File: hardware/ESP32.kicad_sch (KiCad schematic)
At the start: 17 parts, among them J1 GT-USB-7004, SW1 SW_Omron_B3FS, SW2 SW_Omron_B3FS, U1 ESP32-C3-WROOM-02U, U2 VBUS05L1-DD1-G-08, U3 VBUS05L1-DD1-G-08, U4 VBUS05L1-DD1-G-08

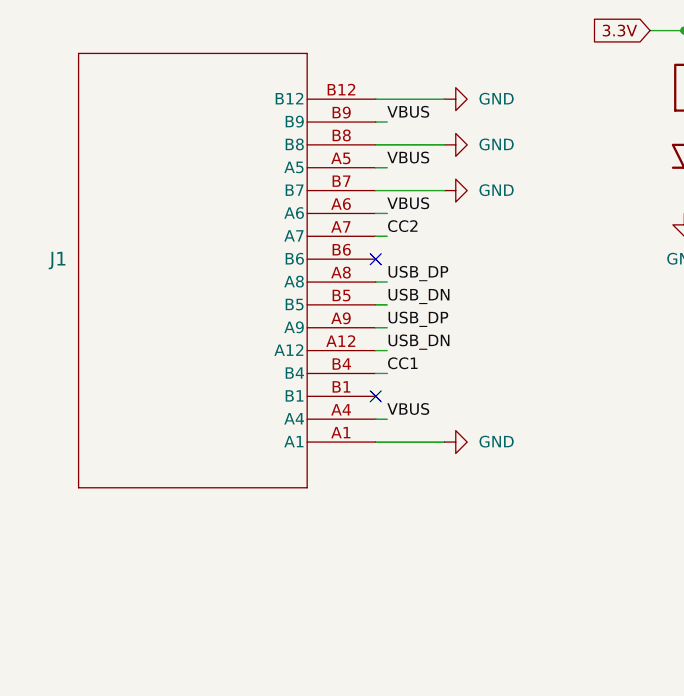
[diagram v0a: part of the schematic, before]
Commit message: New usb port
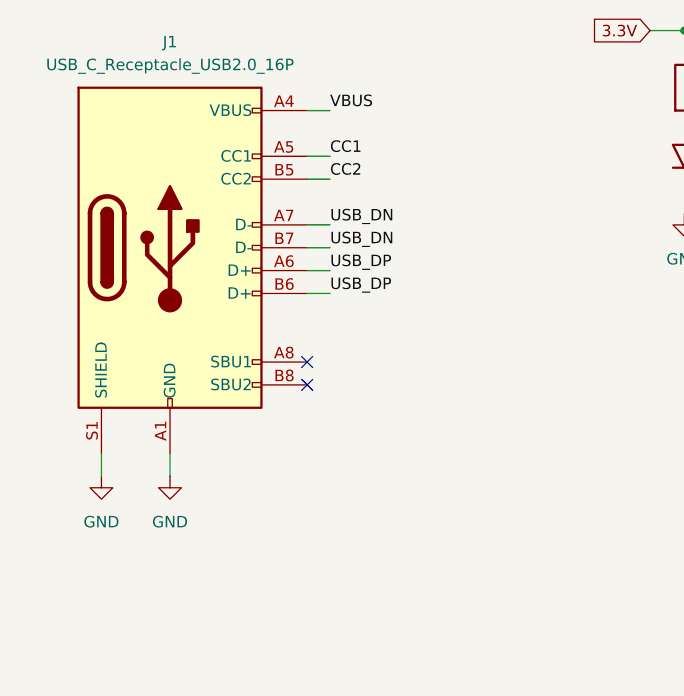
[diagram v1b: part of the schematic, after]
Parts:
- removed J1: GT-USB-7004, GT-USB-7004:CONN12_B-7004_GSW, symbol GT-USB-7004:GT-USB-7004
- added J1: USB_C_Receptacle_USB2.0_16P, Connector_USB:USB_C_Receptacle_GCT_USB4105-xx-A_16P_TopMnt_Horizontal, symbol Connector:USB_C_Receptacle_USB2.0_16P
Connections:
- net CC1: now also J1.A5 (CC1)
- net CC2: now also J1.B5 (CC2)
- net GND: now also J1.A1 (GND), J1.A12 (GND), J1.B1 (GND), J1.B12 (GND), J1.S1 (SHIELD)
- net USB_DN: now also J1.A7 (D-), J1.B7 (D-)
- net USB_DP: now also J1.A6 (D+), J1.B6 (D+)
- net VBUS: now also J1.A4 (VBUS), J1.A9 (VBUS), J1.B4 (VBUS), J1.B9 (VBUS)

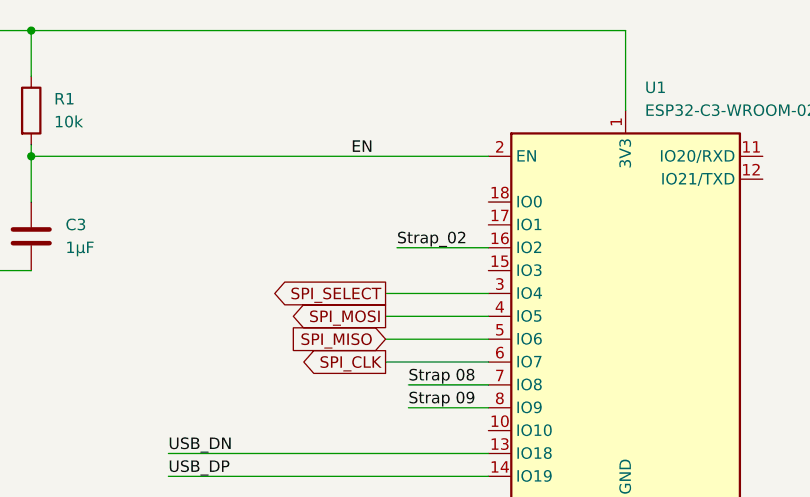
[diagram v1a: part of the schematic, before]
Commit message: Main modules added + Com lines
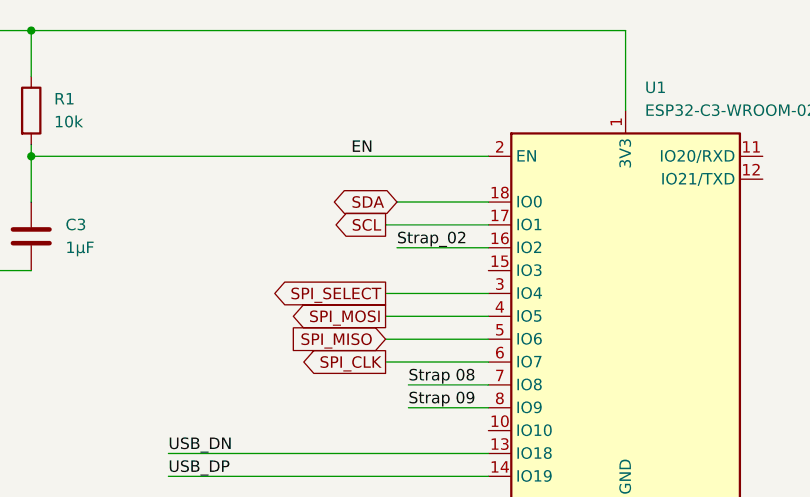
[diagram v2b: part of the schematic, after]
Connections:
- net SCL: now reaches U1.17 (IO1)
- net SDA: now reaches U1.18 (IO0)
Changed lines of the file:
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@@
+	(wire
+		(pts
+			(xy 187.96 50.8) (xy 198.12 50.8)
+		)
+		(stroke
+			(width 0)
+			(type default)
+		)
+	)
 	(wire
 		(pts
@@
 		(pts
 			(xy 129.54 49.53) (xy 134.62 49.53)
+		)
+		(stroke
+			(width 0)
+			(type default)
+		)
+	)
+	(wire
+		(pts
+			(xy 186.69 53.34) (xy 198.12 53.34)
 		)
 		(stroke
@@
 		)
 	)
+	(global_label "SCL"
+		(shape output)
+		(at 186.69 53.34 180)
+		(fields_autoplaced yes)
+		(effects
+			(font
+				(size 1.27 1.27)
+			)
+			(justify right)
+		)
+		(property "Intersheetrefs" "${INTERSHEET_REFS}"
+			(at 180.1972 53.34 0)
+			(effects
+				(font
+					(size 1.27 1.27)
+				)
+				(justify right)
+				(hide yes)
+			)
+		)
+	)
 	(global_label "SPI_MISO"
 		(shape input)
@@
 			(effects
 				(font
+					(size 1.27 1.27)
+				)
+				(justify right)
+				(hide yes)
+			)
+		)
+	)
+	(global_label "SDA"
+		(shape bidirectional)
+		(at 187.96 50.8 180)
+		(fields_autoplaced yes)
+		(effects
+			(font
+				(size 1.27 1.27)
+			)
+			(justify right)
+		)
+		(property "Intersheetrefs" "${INTERSHEET_REFS}"
+			(at 180.2954 50.8 0)
+			(effects
+				(font

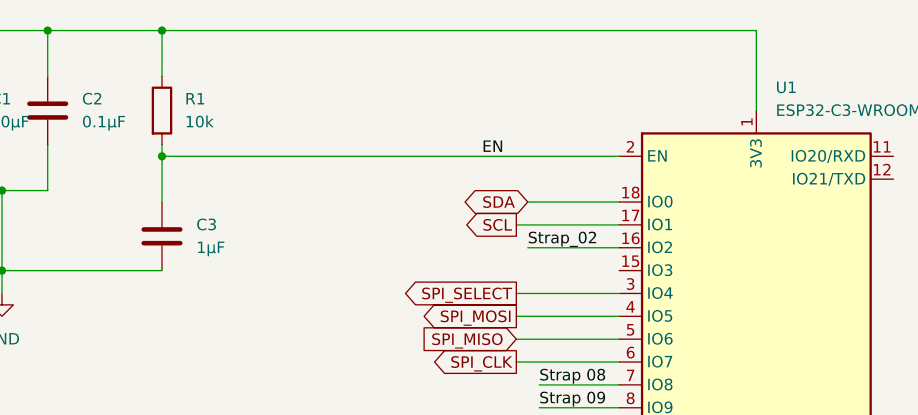
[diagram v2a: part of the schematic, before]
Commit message: Pull up resistor i2c
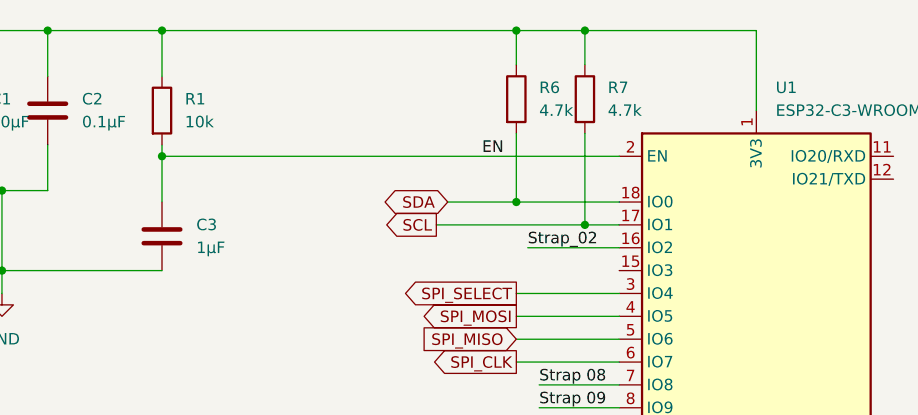
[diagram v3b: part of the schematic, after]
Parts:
- added R6, R7: 4.7k, Resistor_SMD:R_0603_1608Metric, symbol Device:R
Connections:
- net 3.3V: now also R6.1, R7.1
- net SCL: now also R7.2
- net SDA: now also R6.2
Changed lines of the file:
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@@
+	)
+	(junction
+		(at 194.31 31.75)
+		(diameter 0)
+		(color 0 0 0 0)
 	)
 	(junction
@@
 	)
 	(junction
+		(at 194.31 53.34)
+		(diameter 0)
+		(color 0 0 0 0)
+	)
+	(junction
+		(at 186.69 50.8)
+		(diameter 0)
+		(color 0 0 0 0)
+	)
+	(junction
 		(at 124.46 31.75)
 		(diameter 0)
@@
 	)
 	(junction
+		(at 186.69 31.75)
+		(diameter 0)
+		(color 0 0 0 0)
+	)
+	(junction
 		(at 134.62 31.75)
 		(diameter 0)
@@
 	(wire
 		(pts
+			(xy 186.69 31.75) (xy 147.32 31.75)
+		)
+		(stroke
+			(width 0)
+			(type default)
+		)
+	)
+	(wire
+		(pts
+			(xy 186.69 43.18) (xy 186.69 50.8)
+		)
+		(stroke
+			(width 0)
+			(type default)
+		)
+	)
+	(wire
+		(pts
 			(xy 105.41 31.75) (xy 114.3 31.75)
 		)
@@
 	(wire
 		(pts
+			(xy 194.31 31.75) (xy 186.69 31.75)
+		)
+		(stroke
+			(width 0)
+			(type default)
+		)
+	)
+	(wire
+		(pts
 			(xy 162.56 78.74) (xy 198.12 78.74)
 		)
@@
 	(wire
 		(pts
-			(xy 213.36 31.75) (xy 147.32 31.75)
+			(xy 213.36 31.75) (xy 194.31 31.75)
 		)
 		(stroke
@@
 	(wire
 		(pts
-			(xy 187.96 50.8) (xy 198.12 50.8)
+			(xy 179.07 50.8) (xy 186.69 50.8)
 		)
 		(stroke
@@
 	(wire
 		(pts
-			(xy 186.69 53.34) (xy 198.12 53.34)
+			(xy 194.31 31.75) (xy 194.31 35.56)
+		)
+		(stroke
+			(width 0)
+			(type default)
+		)
+	)
+	(wire
+		(pts
+			(xy 177.8 53.34) (xy 194.31 53.34)
+		)
+		(stroke
+			(width 0)
+			(type default)
+		)
+	)
+	(wire
+		(pts
+			(xy 186.69 31.75) (xy 186.69 35.56)
 		)
 		(stroke
@@
 	(wire
 		(pts
+			(xy 186.69 50.8) (xy 198.12 50.8)
+		)
+		(stroke
+			(width 0)
+			(type default)
+		)
+	)
+	(wire
+		(pts
+			(xy 194.31 43.18) (xy 194.31 53.34)
+		)
+		(stroke
+			(width 0)
+			(type default)
+		)
+	)
+	(wire
+		(pts
 			(xy 186.69 63.5) (xy 198.12 63.5)
 		)
@@
 		(pts
 			(xy 147.32 36.83) (xy 147.32 31.75)
+		)
+		(stroke
+			(width 0)
+			(type default)
+		)
+	)
+	(wire
+		(pts
+			(xy 194.31 53.34) (xy 198.12 53.34)
 		)
 		(stroke
@@
 	(global_label "SCL"
 		(shape output)
-		(at 186.69 53.34 180)
+		(at 177.8 53.34 180)
 		(fields_autoplaced yes)
 		(effects
@@
 		)
 		(property "Intersheetrefs" "${INTERSHEET_REFS}"
-			(at 180.1972 53.34 0)
+			(at 171.3072 53.34 0)
 			(effects
 				(font
@@
 	(global_label "SDA"
 		(shape bidirectional)
-		(at 187.96 50.8 180)
+		(at 179.07 50.8 180)
 		(fields_autoplaced yes)
 		(effects
@@
 		)
 		(property "Intersheetrefs" "${INTERSHEET_REFS}"
-			(at 180.2954 50.8 0)
+			(at 171.4054 50.8 0)
 			(effects
 				(font
@@
 				(path "/5b969f6e-a36e-432b-8f00-b2d6a515a877/36e0c9fb-3d9d-4ab1-92fc-4f7433c1320d"
 					(reference "#PWR02")
+					(unit 1)
+				)
+			)
+		)
+	)
+	(symbol
+		(lib_id "Device:R")
+		(at 186.69 39.37 0)
+		(unit 1)
+		(exclude_from_sim no)
+		(in_bom yes)
+		(on_board yes)
+		(dnp no)
+		(fields_autoplaced yes)
+		(property "Reference" "R6"
+			(at 189.23 38.0999 0)
+			(effects
+				(font
+					(size 1.27 1.27)
+				)
+				(justify left)
+			)
+		)
+		(property "Value" "4.7k"
+			(at 189.23 40.6399 0)
+			(effects
+				(font
+					(size 1.27 1.27)
+				)
+				(justify left)
+			)
+		)
+		(property "Footprint" "Resistor_SMD:R_0603_1608Metric"
+			(at 184.912 39.37 90)
+			(effects
+				(font
+					(size 1.27 1.27)
+				)
+				(hide yes)
+			)
+		)
+		(property "Datasheet" "~"
+			(at 186.69 39.37 0)
+			(effects
+				(font
+					(size 1.27 1.27)
+				)
+				(hide yes)
+			)
+		)
+		(property "Description" "Resistor"
+			(at 186.69 39.37 0)
+			(effects
+				(font
+					(size 1.27 1.27)
+				)
+				(hide yes)
+			)
+		)
+		(pin "2"
+		)
+		(pin "1"
+		)
+		(instances
+			(project "GOG"
+				(path "/5b969f6e-a36e-432b-8f00-b2d6a515a877/36e0c9fb-3d9d-4ab1-92fc-4f7433c1320d"
+					(reference "R6")
 					(unit 1)
 				)
@@
 					(unit 1)
 				)
+			)
+		)
+	)
+	(symbol
+		(lib_id "Device:R")
+		(at 194.31 39.37 0)
+		(unit 1)
+		(exclude_from_sim no)
+		(in_bom yes)
+		(on_board yes)
+		(dnp no)
+		(fields_autoplaced yes)
+		(property "Reference" "R7"
+			(at 196.85 38.0999 0)
+			(effects
+				(font
+					(size 1.27 1.27)
+				)
+				(justify left)
+			)
+		)
+		(property "Value" "4.7k"
+			(at 196.85 40.6399 0)
+			(effects
+				(font
+					(size 1.27 1.27)
+				)
+				(justify left)
+			)
+		)
+		(property "Footprint" "Resistor_SMD:R_0603_1608Metric"
+			(at 192.532 39.37 90)
+			(effects
+				(font
+					(size 1.27 1.27)
+				)
+				(hide yes)
+			)
+		)
+		(property "Datasheet" "~"
+			(at 194.31 39.37 0)
+			(effects
+				(font
+					(size 1.27 1.27)
+				)
+				(hide yes)
+			)
+		)
+		(property "Description" "Resistor"
+			(at 194.31 39.37 0)
+			(effects
+				(font
+					(size 1.27 1.27)
+				)
+				(hide yes)
+			)
+		)
+		(pin "2"
+		)
+		(pin "1"
+		)
+		(instances
+			(project "GOG"
+				(path "/5b969f6e-a36e-432b-8f00-b2d6a515a877/36e0c9fb-3d9d-4ab1-92fc-4f7433c1320d"
+					(reference "R7")
+					(unit 1)
+				)

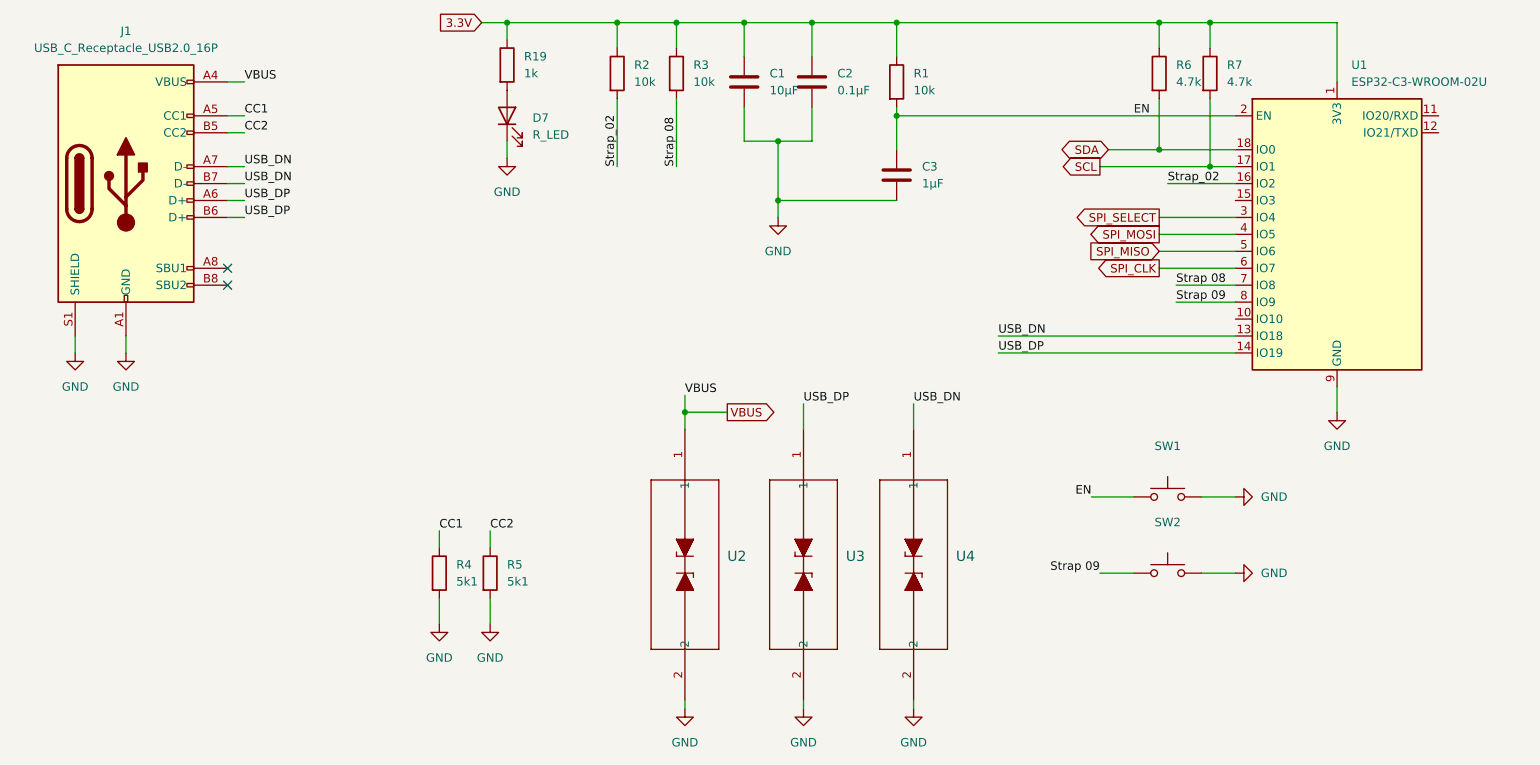
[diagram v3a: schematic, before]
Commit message: ESL protection modification with usblc6 2sc6
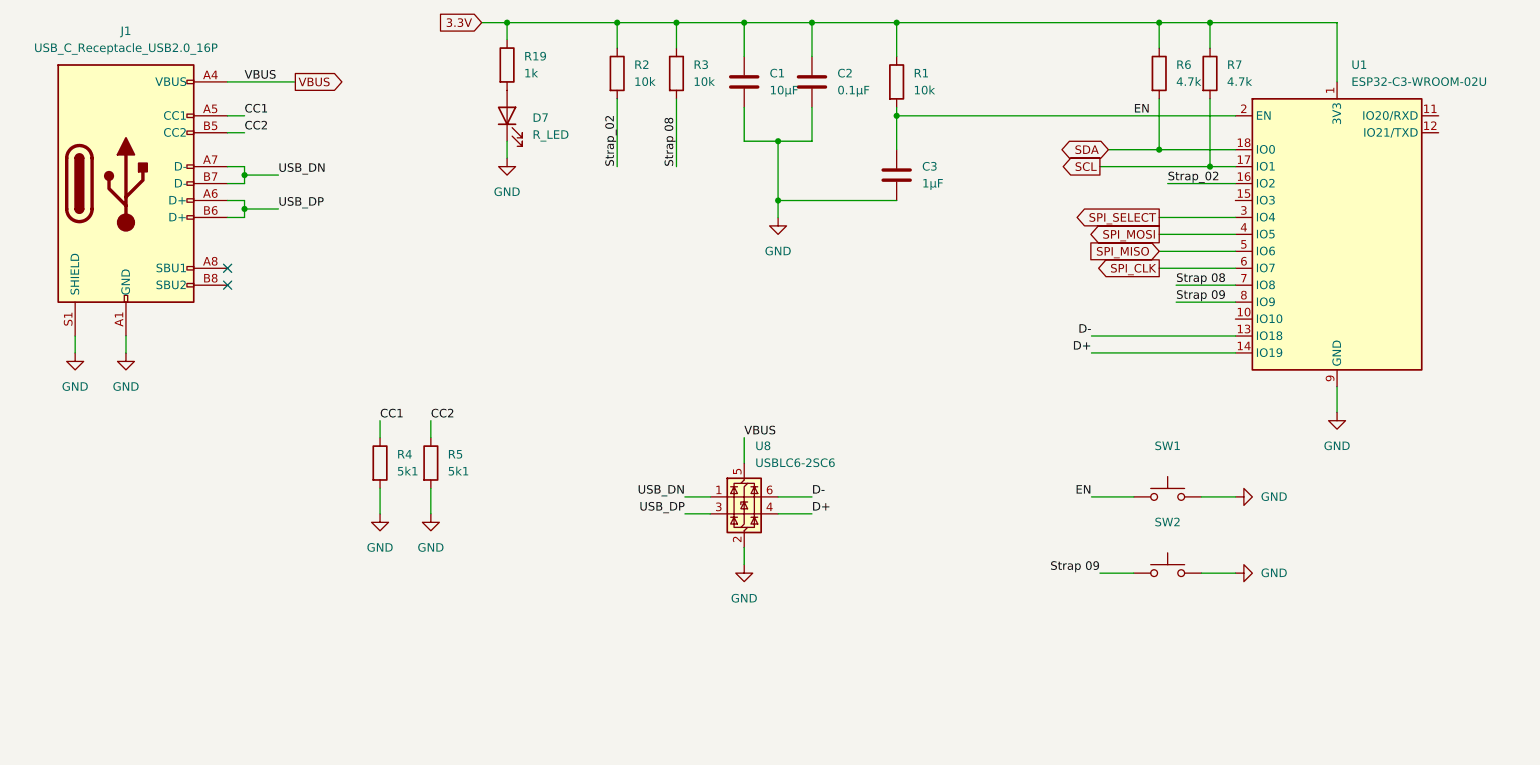
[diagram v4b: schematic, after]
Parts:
- removed U2, U3, U4: VBUS05L1-DD1-G-08, VBUS05L1-DD1-G-08:DIO_LLP1006-2M_VIS, symbol VBUS05L1-DD1-G-08:VBUS05L1-DD1-G-08
- added U8: USBLC6-2SC6, Package_TO_SOT_SMD:SOT-23-6, symbol Power_Protection:USBLC6-2SC6
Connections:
- net GND: now also U8.2 (GND)
- net USB_DN: now also U8.1 (I/O1); no longer U1.13 (IO18)
- net USB_DP: now also U8.3 (I/O2); no longer U1.14 (IO19)
- net VBUS: now also U8.5 (VBUS)
- new net D+: U1.14 (IO19), U8.4 (I/O2)
- new net D-: U1.13 (IO18), U8.6 (I/O1)
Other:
- moved on the sheet: R4, R5

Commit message: Change of esp32 footprint for wifi antenna
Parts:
- removed U1: ESP32-C3-WROOM-02U, RF_Module:ESP32-C3-WROOM-02U, symbol RF_Module:ESP32-C3-WROOM-02U
- added U2: ESP32-C3-WROOM-02, RF_Module:ESP32-C3-WROOM-02, symbol RF_Module:ESP32-C3-WROOM-02
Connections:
- net 3.3V: now also U2.1 (3V3)
- net D+: now also U2.14 (IO19)
- net D-: now also U2.13 (IO18)
- net EN: now also U2.2 (EN)
- net GND: now also U2.19 (GND), U2.9 (GND)
- net SCL: now also U2.17 (IO1)
- net SDA: now also U2.18 (IO0)
- net SPI_CLK: now also U2.6 (IO7)
- net SPI_MISO: now also U2.5 (IO6)
- net SPI_MOSI: now also U2.4 (IO5)
- net SPI_SELECT: now also U2.3 (IO4)
- net Strap 08: now also U2.7 (IO8)
- net Strap 09: now also U2.8 (IO9)
- net Strap_02: now also U2.16 (IO2)
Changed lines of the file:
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@@
-	)
-	(symbol
-		(lib_id "RF_Module:ESP32-C3-WROOM-02U")
-		(at 213.36 63.5 0)
-		(unit 1)
-		(exclude_from_sim no)
-		(in_bom yes)
-		(on_board yes)
-		(dnp no)
-		(fields_autoplaced yes)
-		(property "Reference" "U1"
-			(at 215.5033 38.1 0)
-			(effects
-				(font
-					(size 1.27 1.27)
-				)
-				(justify left)
-			)
-		)
-		(property "Value" "ESP32-C3-WROOM-02U"
-			(at 215.5033 40.64 0)
-			(effects
-				(font
-					(size 1.27 1.27)
-				)
-				(justify left)
-			)
-		)
-		(property "Footprint" "RF_Module:ESP32-C3-WROOM-02U"
-			(at 213.36 64.135 0)
-			(effects
-				(font
-					(size 1.27 1.27)
-				)
-				(hide yes)
-			)
-		)
-		(property "Datasheet" "https://www.espressif.com/sites/default/files/documentation/esp32-c3-wroom-02_datasheet_en.pdf"
-			(at 213.36 64.135 0)
-			(effects
-				(font
-					(size 1.27 1.27)
-				)
-				(hide yes)
-			)
-		)
-		(property "Description" "802.11 b/g/n Wi­Fi and Bluetooth 5 module, ESP32­C3 SoC, RISC­V microprocessor, On-board antenna"
-			(at 213.36 64.135 0)
-			(effects
-				(font
-					(size 1.27 1.27)
-				)
-				(hide yes)
-			)
-		)
-		(pin "3"
-		)
-		(pin "2"
-		)
-		(pin "18"
-		)
-		(pin "17"
-		)
-		(pin "5"
-		)
-		(pin "4"
-		)
-		(pin "10"
-		)
-		(pin "8"
-		)
-		(pin "15"
-		)
-		(pin "7"
-		)
-		(pin "16"
-		)
-		(pin "6"
-		)
-		(pin "14"
-		)
-		(pin "1"
-		)
-		(pin "13"
-		)
-		(pin "19"
-		)
-		(pin "11"
-		)
-		(pin "9"
-		)
-		(pin "12"
-		)
-		(instances
-			(project ""
-				(path "/5b969f6e-a36e-432b-8f00-b2d6a515a877/36e0c9fb-3d9d-4ab1-92fc-4f7433c1320d"
-					(reference "U1")
-					(unit 1)
-				)
-			)
-		)
 	)
 	(symbol
@@
 					(unit 1)
 				)
+			)
+		)
+	)
+	(symbol
+		(lib_id "RF_Module:ESP32-C3-WROOM-02")
+		(at 213.36 63.5 0)
+		(unit 1)
+		(exclude_from_sim no)
+		(in_bom yes)
+		(on_board yes)
+		(dnp no)
+		(fields_autoplaced yes)
+		(property "Reference" "U2"
+			(at 215.5033 38.1 0)
+			(effects
+				(font
+					(size 1.27 1.27)
+				)
+				(justify left)
+			)
+		)
+		(property "Value" "ESP32-C3-WROOM-02"
+			(at 215.5033 40.64 0)
+			(effects
+				(font
+					(size 1.27 1.27)
+				)
+				(justify left)
+			)
+		)
+		(property "Footprint" "RF_Module:ESP32-C3-WROOM-02"
+			(at 213.36 62.865 0)
+			(effects
+				(font
+					(size 1.27 1.27)
+				)
+				(hide yes)
+			)
+		)
+		(property "Datasheet" "https://www.espressif.com/sites/default/files/documentation/esp32-c3-wroom-02_datasheet_en.pdf"
+			(at 213.36 62.865 0)
+			(effects
+				(font
+					(size 1.27 1.27)
+				)
+				(hide yes)
+			)
+		)
+		(property "Description" "802.11 b/g/n Wi­Fi and Bluetooth 5 module, ESP32­C3 SoC, RISC­V microprocessor, On-board antenna"
+			(at 213.36 62.865 0)
+			(effects
+				(font
+					(size 1.27 1.27)
+				)
+				(hide yes)
+			)
+		)
+		(pin "17"
+		)
+		(pin "4"
+		)
+		(pin "16"
+		)
+		(pin "2"
+		)
+		(pin "18"
+		)
+		(pin "15"
+		)
+		(pin "3"
+		)
+		(pin "19"
+		)
+		(pin "13"
+		)
+		(pin "14"
+		)
+		(pin "11"
+		)
+		(pin "1"
+		)
+		(pin "10"
+		)
+		(pin "6"
+		)
+		(pin "9"
+		)
+		(pin "8"
+		)
+		(pin "5"
+		)
+		(pin "12"
+		)
+		(pin "7"
+		)
+		(instances
+			(project ""
+				(path "/5b969f6e-a36e-432b-8f00-b2d6a515a877/36e0c9fb-3d9d-4ab1-92fc-4f7433c1320d"
+					(reference "U2")
+					(unit 1)
+				)
